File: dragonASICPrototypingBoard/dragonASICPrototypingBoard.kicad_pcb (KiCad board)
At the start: 2 copper layers, 68.6 x 53.3 mm, 8 parts, among them P1 Power, P2 Analog, P3 Digital, P4 Digital, P5 CONN_1, P6 CONN_1, P7 CONN_1, P8 CONN_1

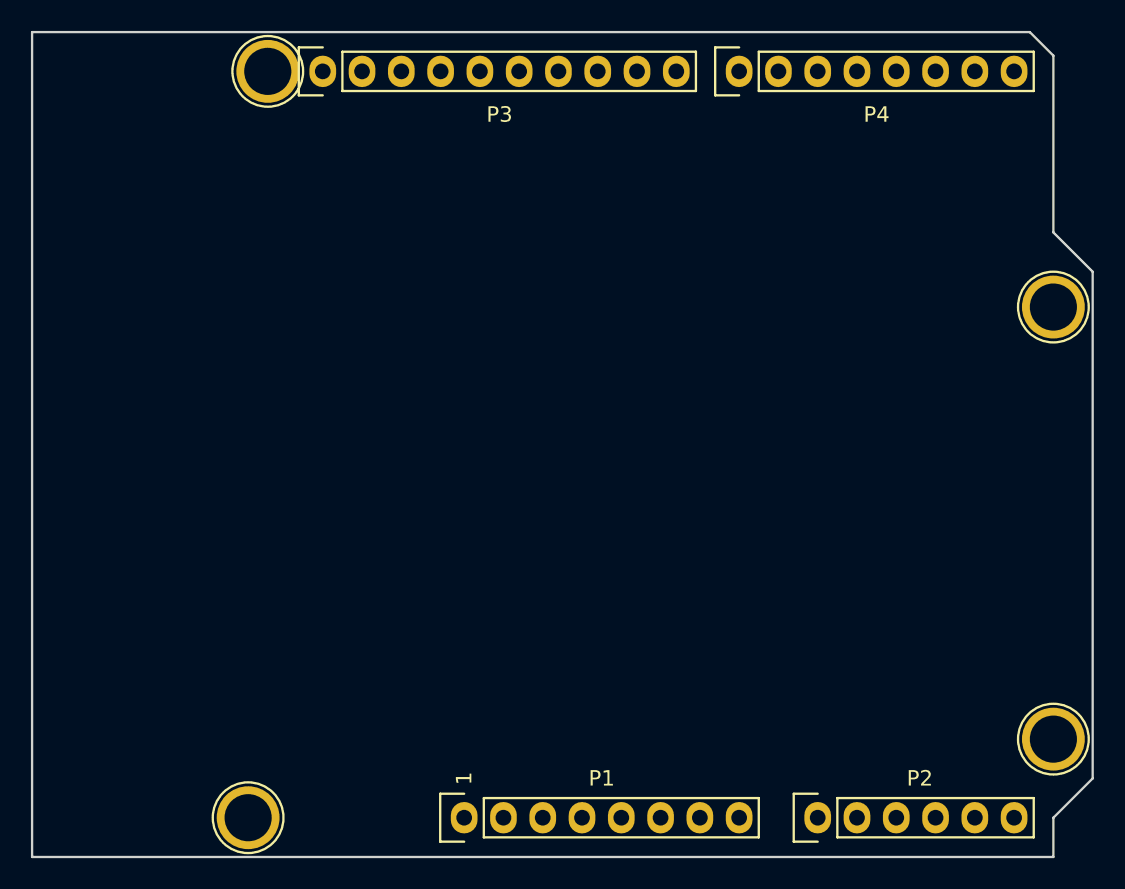
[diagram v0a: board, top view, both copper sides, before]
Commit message: Add PCB layout to dragonASICPrototypingBoard
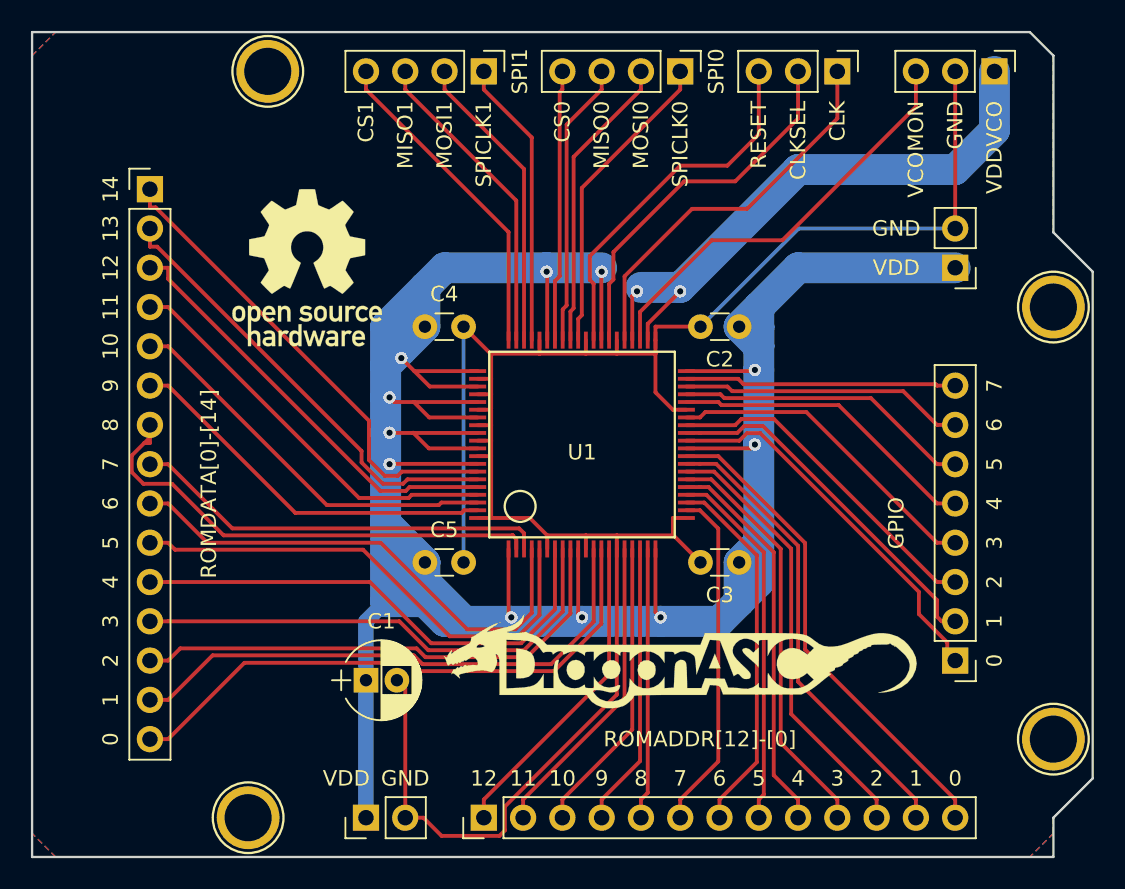
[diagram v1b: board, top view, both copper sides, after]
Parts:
- removed P1: Power, Socket_Arduino_Uno:Socket_Strip_Arduino_1x08
- removed P2: Analog, Socket_Arduino_Uno:Socket_Strip_Arduino_1x06
- removed P3: Digital, Socket_Arduino_Uno:Socket_Strip_Arduino_1x10
- removed P4: Digital, Socket_Arduino_Uno:Socket_Strip_Arduino_1x08
- added ?: CONN_01X08, Pin_Headers:Pin_Header_Straight_1x08_Pitch2.54mm, F.Cu at (170.7, 113.7)
- added ?: CONN_01X03, Pin_Headers:Pin_Header_Straight_1x03_Pitch2.54mm, F.Cu at (163.1, 75.6)
- added ?: CONN_01X02, Pin_Headers:Pin_Header_Straight_1x02_Pitch2.54mm, F.Cu at (170.7, 88.3)
- added ?: CONN_01X02, Pin_Headers:Pin_Header_Straight_1x02_Pitch2.54mm, F.Cu at (132.6, 123.8)
- added ?: CONN_01X13, Pin_Headers:Pin_Header_Straight_1x13_Pitch2.54mm, F.Cu at (140.2, 123.8)
- added ?: CONN_01X15, Pin_Headers:Pin_Header_Straight_1x15_Pitch2.54mm, F.Cu at (118.6, 83.2)
- added ?: CONN_01X03, Pin_Headers:Pin_Header_Straight_1x03_Pitch2.54mm, F.Cu at (173.2, 75.6)
- added C1: CP, Capacitors_ThroughHole:CP_Radial_D5.0mm_P2.00mm, F.Cu at (132.6, 114.9)
- added C2: C, Capacitors_ThroughHole:C_Disc_D3.0mm_W1.6mm_P2.50mm, F.Cu at (156.7, 92.1)
- added C3: C, Capacitors_ThroughHole:C_Disc_D3.0mm_W1.6mm_P2.50mm, F.Cu at (156.7, 107.3)
- added C4: C, Capacitors_ThroughHole:C_Disc_D3.0mm_W1.6mm_P2.50mm, F.Cu at (136.4, 92.1)
- added C5: C, Capacitors_ThroughHole:C_Disc_D3.0mm_W1.6mm_P2.50mm, F.Cu at (136.4, 107.3)
- added G***: LOGO, dragonASICPrototypingBoard:logoPrototypingBoard, F.Cu at (152.9, 113.7)
- added G***: LOGO, dragonASICPrototypingBoard:logoOpenSource, F.Cu at (128.8, 88.3)
- added SPI0: CONN_01X04, Pin_Headers:Pin_Header_Straight_1x04_Pitch2.54mm, F.Cu at (152.9, 75.6)
- added SPI1: CONN_01X04, Pin_Headers:Pin_Header_Straight_1x04_Pitch2.54mm, F.Cu at (140.2, 75.6)
- added U1: QFP80, dragonASICPrototypingBoard:QFP80, F.Cu at (146.6, 99.7)
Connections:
- P5 pad 1: Net-(P5-Pad1) -> (no net)
- P6 pad 1: Net-(P6-Pad1) -> (no net)
- P7 pad 1: Net-(P7-Pad1) -> (no net)
- P8 pad 1: Net-(P8-Pad1) -> (no net)
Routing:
- net /VDD: track 0.00 -> 208.2 mm, vias 0 -> 11
- net /GND: track 0.00 -> 143.4 mm
- net Net-(U1-Pad42): track 0.00 -> 39.0 mm, vias 0 -> 2
- net /ROMDATA[0]: track 0.00 -> 37.6 mm
- net /ROMDATA[1]: track 0.00 -> 36.0 mm
- net /ROMDATA[2]: track 0.00 -> 33.1 mm
- net /ROMDATA[4]: track 0.00 -> 32.6 mm
- net /ROMDATA[6]: track 0.00 -> 32.6 mm
- net /ROMDATA[3]: track 0.00 -> 32.5 mm
- net /ROMDATA[5]: track 0.00 -> 32.5 mm
- net /ROMDATA[8]: track 0.00 -> 32.4 mm
- net /ROMADDR[0]: track 0.00 -> 31.8 mm
- net /ROMDATA[14]: track 0.00 -> 31.2 mm
- net /ROMADDR[1]: track 0.00 -> 30.2 mm
- net /ROMDATA[13]: track 0.00 -> 29.3 mm
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- added copper zone on B.Cu, net /GND
- added copper zone on F.Cu, net /GND
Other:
- board text added: "0"
- board text added: "10"
- board text added: "11"
- board text added: "12"
- board text added: "13"
- board text added: "14"
- board text added: "2"
- board text added: "3"
- board text added: "4"
- board text added: "5"
- board text added: "6"
- board text added: "7"
- board text added: "8"
- board text added: "9"
- board text added: "CLK"
- board text added: "CLKSEL"
- board text added: "CS0"
- board text added: "CS1"
- board text added: "GND"
- board text added: "GPIO"
- board text added: "MISO0"
- board text added: "MISO1"
- board text added: "MOSI0"
- board text added: "MOSI1"
- board text added: "RESET"
- board text added: "ROMADDR[12]-[0]"
- board text added: "ROMDATA[0]-[14]"
- board text added: "SPICLK0"
- board text added: "SPICLK1"
- board text added: "VCOMON"
- board text added: "VDD"
- board text added: "VDDVCO"
